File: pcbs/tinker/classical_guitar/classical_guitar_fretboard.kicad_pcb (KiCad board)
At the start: 2 copper layers, 188 parts, among them Q1 AO3401A, U1 AT42QT1110-A, U2 AT42QT1110-A, U3 AT42QT1110-A, U4 MP2359

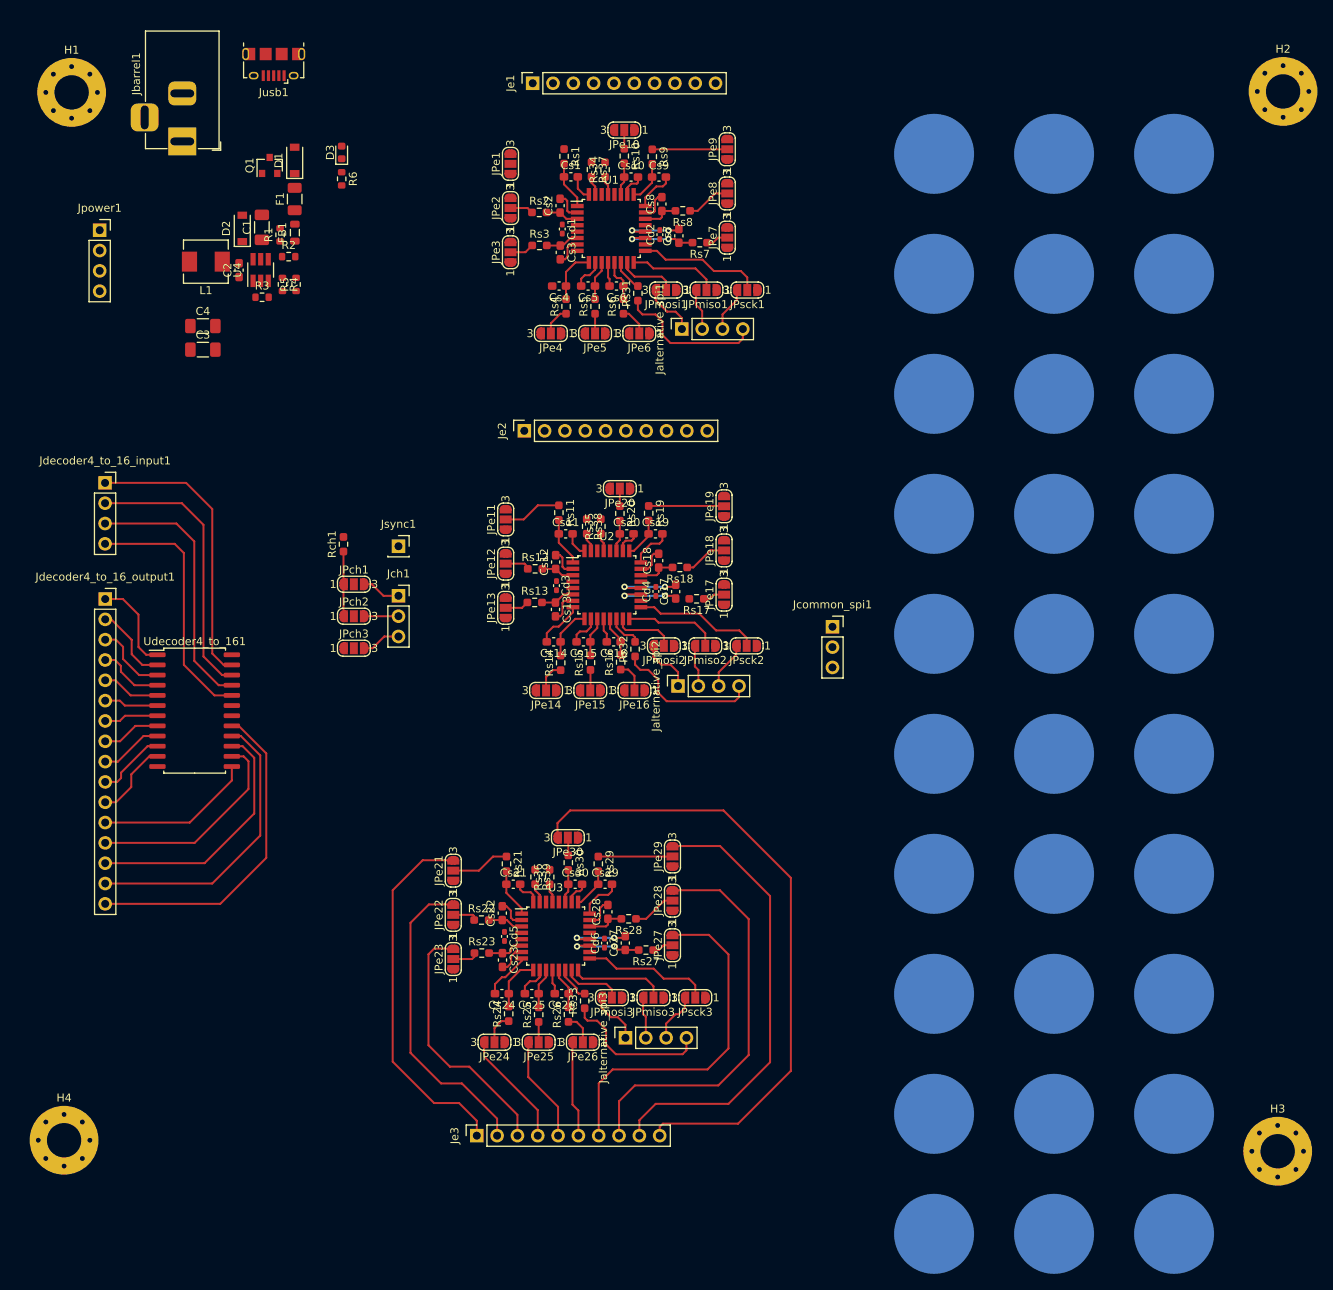
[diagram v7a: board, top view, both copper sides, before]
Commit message: Testing blind vias
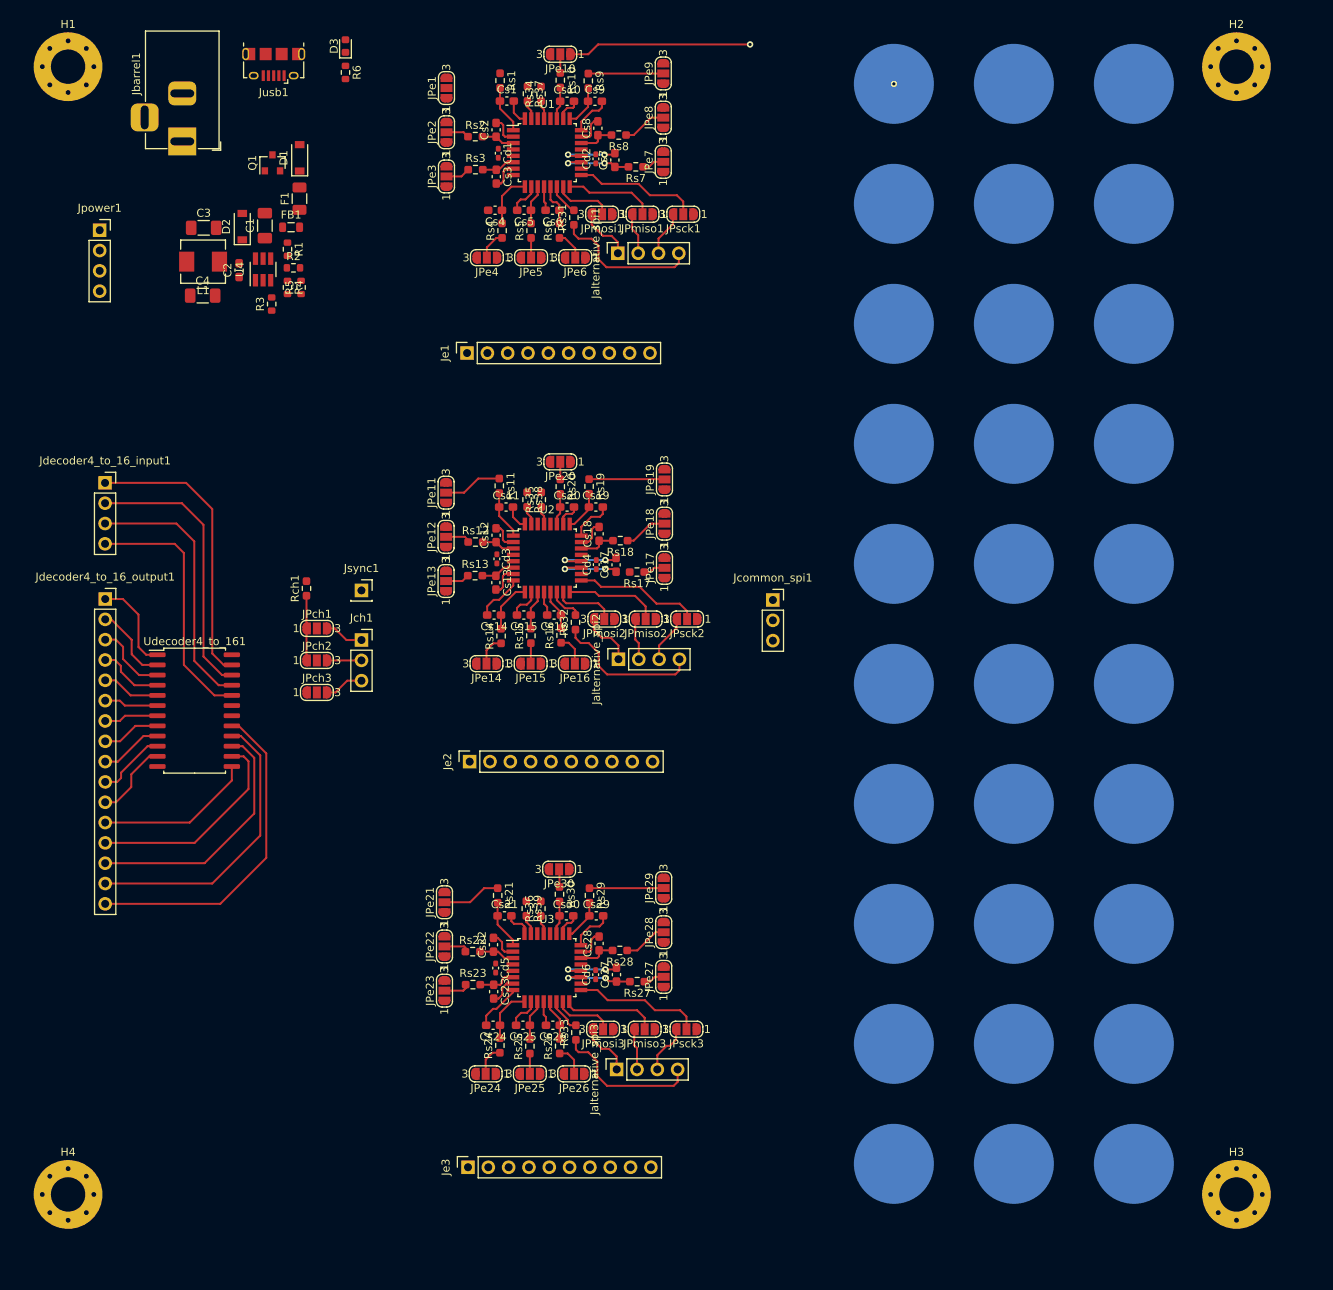
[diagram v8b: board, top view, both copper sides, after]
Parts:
- moved Je2 41.9 mm to (82.0, 104.7)
- moved Je1 34.7 mm to (81.6, 53.6)
- moved C3 15.2 mm to (48.7, 37.9)
- moved D3 13.3 mm to (66.4, 15.2)
- moved R6 13.3 mm to (66.4, 18.5)
- moved Cd1 12.4 mm to (85.5, 28.6)
- moved Cs1 12.4 mm to (86.6, 22.1)
- moved Cs3 12.4 mm to (85.3, 31.5)
- moved Cs4 12.4 mm to (85.1, 35.7)
- moved Cs5 12.4 mm to (88.8, 35.7)
- moved Cs6 12.4 mm to (92.3, 35.7)
- moved Cs8 12.4 mm to (98.0, 25.5)
- moved JPe1 12.4 mm to (79.0, 20.4)
- moved JPe2 12.4 mm to (79.0, 26.0)
- moved JPe3 12.4 mm to (79.0, 31.5)
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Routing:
- net Net-(JPe30-Pad3): track 79.7 -> 0.00 mm
- net Net-(JPe29-Pad3): track 56.8 -> 0.00 mm
- net Net-(JPe28-Pad3): track 50.9 -> 0.00 mm
- net Net-(JPe21-Pad3): track 46.0 -> 0.00 mm
- net Net-(JPe27-Pad3): track 44.3 -> 0.00 mm
- net Net-(E10-Pad1): track 0.00 -> 42.9 mm, vias 0 -> 2
- net Net-(JPe22-Pad3): track 38.9 -> 0.00 mm
- net Net-(JPe23-Pad3): track 32.1 -> 0.00 mm
- net Net-(JPe24-Pad3): track 14.5 -> 0.00 mm
- net Net-(JPe25-Pad3): track 13.2 -> 0.00 mm
- net Net-(JPe26-Pad3): track 12.0 -> 0.00 mm
- added copper zone on In1.Cu, net GND
- added copper zone on In2.Cu, net VDD
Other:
- copper layers 2 -> 4
